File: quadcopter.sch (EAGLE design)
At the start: 6 parts, among them J1 AVR_SPI_PRG_6NS, U1 ATMEGA128RFA1

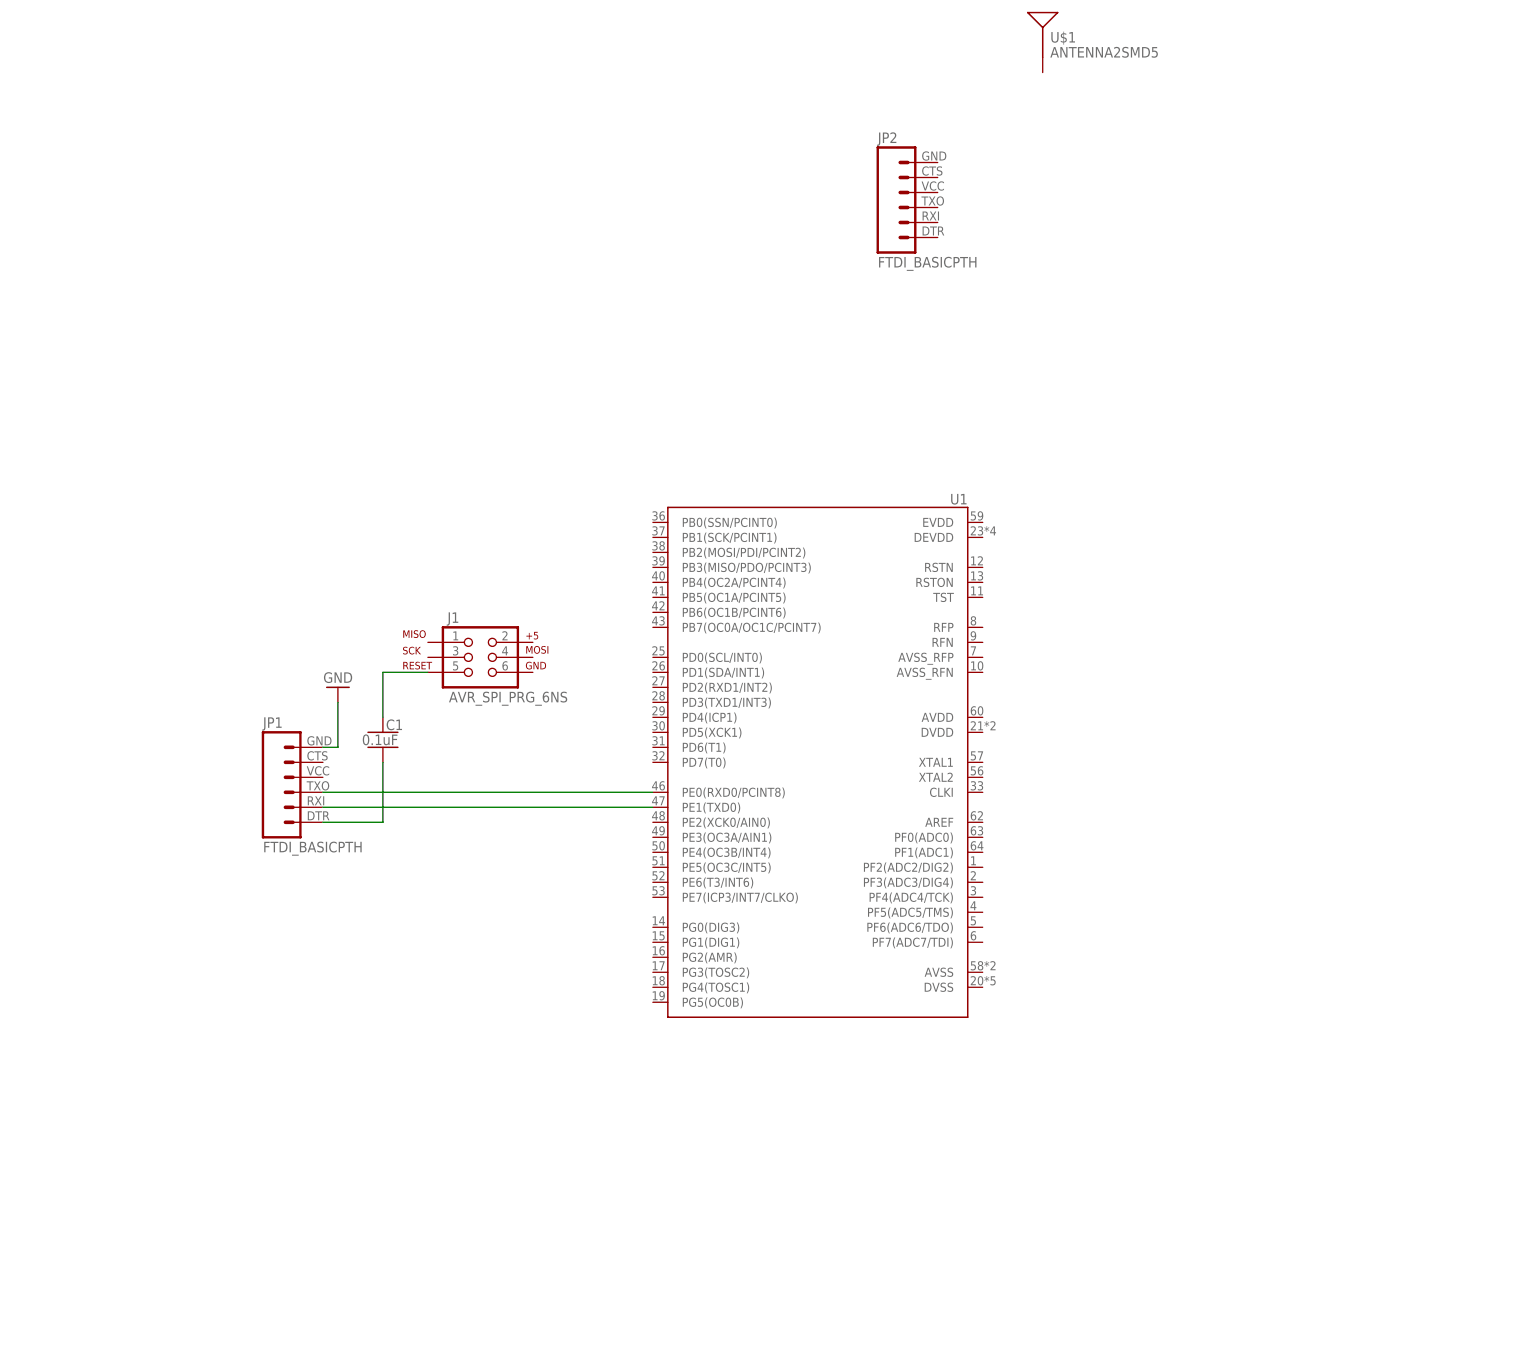
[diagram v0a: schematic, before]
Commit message: updated quadcopter schematic
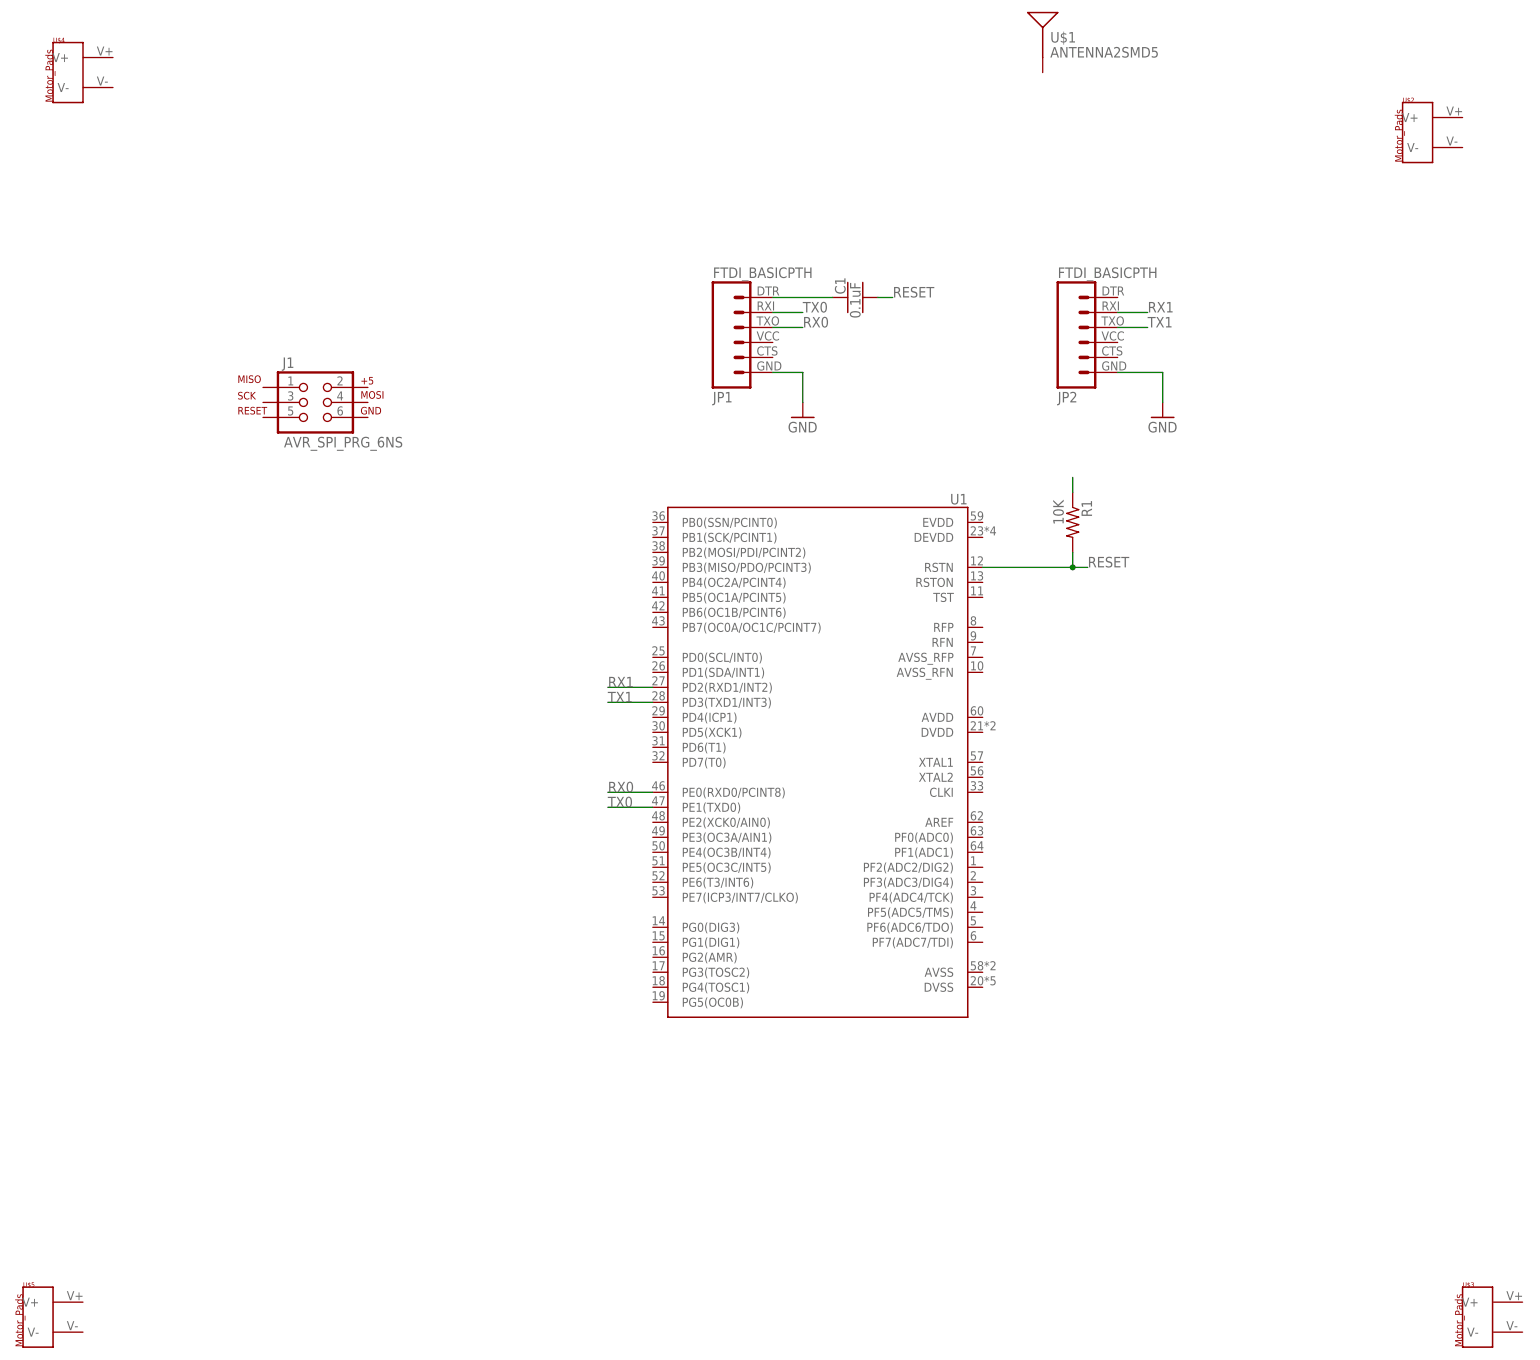
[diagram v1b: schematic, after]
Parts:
- added R1: 10K, quadparts_prebuilt:RESISTOR_SMD-2012-0805-10K
- added U$2, U$3, U$4, U$5: MOTOR_PADS, quadparts_prebuilt:MOTOR_PADS
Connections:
- new net N$5: R1.1
- new net N$6: JP2.2
- new net N$7: JP2.3
- new net RESET: R1.2, U1.RSTN
- new net RX0: U1.PE0(RXD0/PCINT8)
- new net RX1: U1.PD2(RXD1/INT2)
- new net TX0: U1.PE1(TXD0)
- new net TX1: U1.PD3(TXD1/INT3)
- net GND: now also JP2.6
- net N$1: now also C1.1, JP1.1; no longer JP1.2, U1.PE1(TXD0)
- net N$2: no longer U1.PE0(RXD0/PCINT8)
- net N$3: now also JP1.2; no longer C1.2, JP1.1
- net N$4: now also C1.2; no longer C1.1, J1.5
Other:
- moved on the sheet: C1, J1, JP1, JP2
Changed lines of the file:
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@@
 <part name="GND1" library="quadparts_prebuilt" deviceset="GND" device=""/>
 <part name="C1" library="quadparts_connie" deviceset="CERAMIC_CAP" device="-0805-0.1UF" value="0.1uF"/>
+<part name="U$2" library="quadparts_prebuilt" deviceset="MOTOR_PADS" device=""/>
+<part name="U$3" library="quadparts_prebuilt" deviceset="MOTOR_PADS" device=""/>
+<part name="U$4" library="quadparts_prebuilt" deviceset="MOTOR_PADS" device=""/>
+<part name="U$5" library="quadparts_prebuilt" deviceset="MOTOR_PADS" device=""/>
+<part name="R1" library="quadparts_prebuilt" deviceset="RESISTOR_" device="SMD-2012-0805-10K" value="10K"/>
+<part name="GND2" library="quadparts_prebuilt" deviceset="GND" device=""/>
 </parts>
 <sheets>
@@
 <instances>
 <instance part="U1" gate="G$1" x="-58.42" y="-60.96" rot="MR0"/>
-<instance part="JP1" gate="G$1" x="-147.32" y="-66.04"/>
-<instance part="JP2" gate="G$1" x="-43.18" y="33.02"/>
-<instance part="J1" gate="G$1" x="-116.84" y="-43.18"/>
+<instance part="JP1" gate="G$1" x="-71.12" y="12.7" rot="MR180"/>
+<instance part="JP2" gate="G$1" x="-12.7" y="12.7" rot="MR180"/>
+<instance part="J1" gate="G$1" x="-144.78" y="0"/>
 <instance part="U$1" gate="G$1" x="-20.32" y="60.96"/>
-<instance part="GND1" gate="1" x="-139.7" y="-48.26" rot="R180"/>
-<instance part="C1" gate="G$1" x="-132.08" y="-55.88"/>
+<instance part="GND1" gate="1" x="-60.96" y="-2.54"/>
+<instance part="C1" gate="G$1" x="-53.34" y="17.78" rot="R90"/>
+<instance part="U$2" gate="G$1" x="43.18" y="43.18"/>
+<instance part="U$3" gate="G$1" x="53.34" y="-157.48"/>
+<instance part="U$4" gate="G$1" x="-185.42" y="53.34"/>
+<instance part="U$5" gate="G$1" x="-190.5" y="-157.48"/>
+<instance part="R1" gate="G$1" x="-15.24" y="-20.32" rot="R270"/>
+<instance part="GND2" gate="1" x="0" y="-2.54"/>
 </instances>
 <busses>
 </busses>
 <nets>
-<net name="N$1" class="0">
+<net name="GND" class="0">
 <segment>
-<pinref part="JP1" gate="G$1" pin="2"/>
-<pinref part="U1" gate="G$1" pin="PE1(TXD0)"/>
-<wire x1="-142.24" y1="-68.58" x2="-86.36" y2="-68.58" width="0.1524" layer="91"/>
+<pinref part="JP1" gate="G$1" pin="6"/>
+<wire x1="-66.04" y1="5.08" x2="-60.96" y2="5.08" width="0.1524" layer="91"/>
+<pinref part="GND1" gate="1" pin="GND"/>
+<wire x1="-60.96" y1="5.08" x2="-60.96" y2="0" width="0.1524" layer="91"/>
+</segment>
+<segment>
+<pinref part="JP2" gate="G$1" pin="6"/>
+<pinref part="GND2" gate="1" pin="GND"/>
+<wire x1="-7.62" y1="5.08" x2="0" y2="5.08" width="0.1524" layer="91"/>
+<wire x1="0" y1="5.08" x2="0" y2="0" width="0.1524" layer="91"/>
 </segment>
 </net>
@@
 <segment>
 <pinref part="JP1" gate="G$1" pin="3"/>
-<pinref part="U1" gate="G$1" pin="PE0(RXD0/PCINT8)"/>
-<wire x1="-142.24" y1="-66.04" x2="-86.36" y2="-66.04" width="0.1524" layer="91"/>
+<wire x1="-66.04" y1="12.7" x2="-60.96" y2="12.7" width="0.1524" layer="91"/>
 </segment>
 </net>
-<net name="GND" class="0">
+<net name="RX0" class="0">
 <segment>
-<pinref part="JP1" gate="G$1" pin="6"/>
-<pinref part="GND1" gate="1" pin="GND"/>
-<wire x1="-142.24" y1="-58.42" x2="-139.7" y2="-58.42" width="0.1524" layer="91"/>
-<wire x1="-139.7" y1="-58.42" x2="-139.7" y2="-50.8" width="0.1524" layer="91"/>
+<pinref part="U1" gate="G$1" pin="PE0(RXD0/PCINT8)"/>
+<wire x1="-86.36" y1="-66.04" x2="-93.98" y2="-66.04" width="0.1524" layer="91"/>
+<label x="-60.96" y="12.7" size="1.778" layer="95"/>
+<label x="-93.98" y="-66.04" size="1.778" layer="95"/>
+</segment>
+</net>
+<net name="TX0" class="0">
+<segment>
+<pinref part="U1" gate="G$1" pin="PE1(TXD0)"/>
+<wire x1="-86.36" y1="-68.58" x2="-93.98" y2="-68.58" width="0.1524" layer="91"/>
+<label x="-60.96" y="15.24" size="1.778" layer="95"/>
+<label x="-93.98" y="-68.58" size="1.778" layer="95"/>
 </segment>
 </net>
 <net name="N$3" class="0">
 <segment>
+<pinref part="JP1" gate="G$1" pin="2"/>
+<wire x1="-66.04" y1="15.24" x2="-60.96" y2="15.24" width="0.1524" layer="91"/>
+</segment>
+</net>
+<net name="N$1" class="0">
+<segment>
 <pinref part="JP1" gate="G$1" pin="1"/>
-<wire x1="-142.24" y1="-71.12" x2="-132.08" y2="-71.12" width="0.1524" layer="91"/>
-<pinref part="C1" gate="G$1" pin="2"/>
-<wire x1="-132.08" y1="-71.12" x2="-132.08" y2="-60.96" width="0.1524" layer="91"/>
+<pinref part="C1" gate="G$1" pin="1"/>
+<wire x1="-66.04" y1="17.78" x2="-55.88" y2="17.78" width="0.1524" layer="91"/>
 </segment>
 </net>
 <net name="N$4" class="0">
 <segment>
-<pinref part="C1" gate="G$1" pin="1"/>
-<wire x1="-132.08" y1="-53.34" x2="-132.08" y2="-45.72" width="0.1524" layer="91"/>
-<pinref part="J1" gate="G$1" pin="5"/>
-<wire x1="-132.08" y1="-45.72" x2="-124.46" y2="-45.72" width="0.1524" layer="91"/>
+<pinref part="C1" gate="G$1" pin="2"/>
+<wire x1="-48.26" y1="17.78" x2="-45.72" y2="17.78" width="0.1524" layer="91"/>
 </segment>
 </net>
+<net name="RESET" class="0">
+<segment>
+<pinref part="U1" gate="G$1" pin="RSTN"/>
+<wire x1="-30.48" y1="-27.94" x2="-15.24" y2="-27.94" width="0.1524" layer="91"/>
+<junction x="-15.24" y="-27.94"/>
+<wire x1="-15.24" y1="-27.94" x2="-12.7" y2="-27.94" width="0.1524" layer="91"/>
+<label x="-45.72" y="17.78" size="1.778" layer="95"/>
+<label x="-12.7" y="-27.94" size="1.778" layer="95"/>
+<pinref part="R1" gate="G$1" pin="2"/>
+<wire x1="-15.24" y1="-25.4" x2="-15.24" y2="-27.94" width="0.1524" layer="91"/>
+</segment>
+</net>
+<net name="N$5" class="0">
+<segment>
+<pinref part="R1" gate="G$1" pin="1"/>
+<wire x1="-15.24" y1="-15.24" x2="-15.24" y2="-12.7" width="0.1524" layer="91"/>
+</segment>
+</net>
+<net name="N$6" class="0">
+<segment>
+<pinref part="JP2" gate="G$1" pin="2"/>
+<wire x1="-7.62" y1="15.24" x2="-2.54" y2="15.24" width="0.1524" layer="91"/>
+</segment>
+</net>
+<net name="N$7" class="0">
+<segment>
+<pinref part="JP2" gate="G$1" pin="3"/>
+<wire x1="-7.62" y1="12.7" x2="-2.54" y2="12.7" width="0.1524" layer="91"/>
+</segment>
+</net>
+<net name="RX1" class="0">
+<segment>
+<pinref part="U1" gate="G$1" pin="PD2(RXD1/INT2)"/>
+<wire x1="-86.36" y1="-48.26" x2="-93.98" y2="-48.26" width="0.1524" layer="91"/>
+<label x="-2.54" y="15.24" size="1.778" layer="95"/>
+<label x="-93.98" y="-48.26" size="1.778" layer="95"/>
+</segment>
+</net>
+<net name="TX1" class="0">
+<segment>
+<pinref part="U1" gate="G$1" pin="PD3(TXD1/INT3)"/>
+<wire x1="-86.36" y1="-50.8" x2="-93.98" y2="-50.8" width="0.1524" layer="91"/>
+<label x="-2.54" y="12.7" size="1.778" layer="95"/>
+<label x="-93.98" y="-50.8" size="1.778" layer="95"/>
+</segment>
+</net>
